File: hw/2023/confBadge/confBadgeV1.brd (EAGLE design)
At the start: 96.5 x 78.7 mm, 70 parts, among them J1 10118192-0002LF, Q1 8/16/20MHz, U1 ATMEGA328, U10 WS2812-2020, U11 WS2812-2020, U12 WS2812-2020, U13 WS2812-2020, U14 WS2812-2020, U15 WS2812-2020, U16 WS2812-2020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

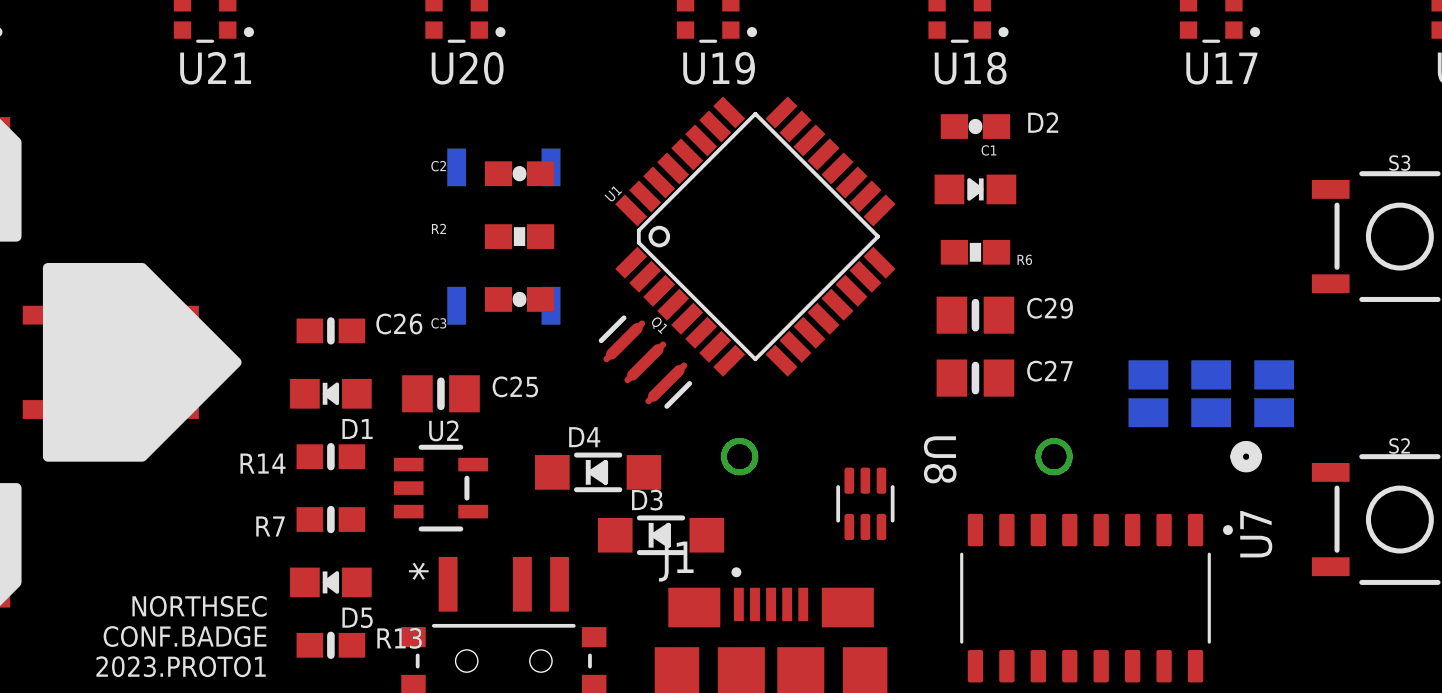
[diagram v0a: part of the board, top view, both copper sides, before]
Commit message: Tested monochrome bitmap
Added Rao to the back of the confBadge for testing
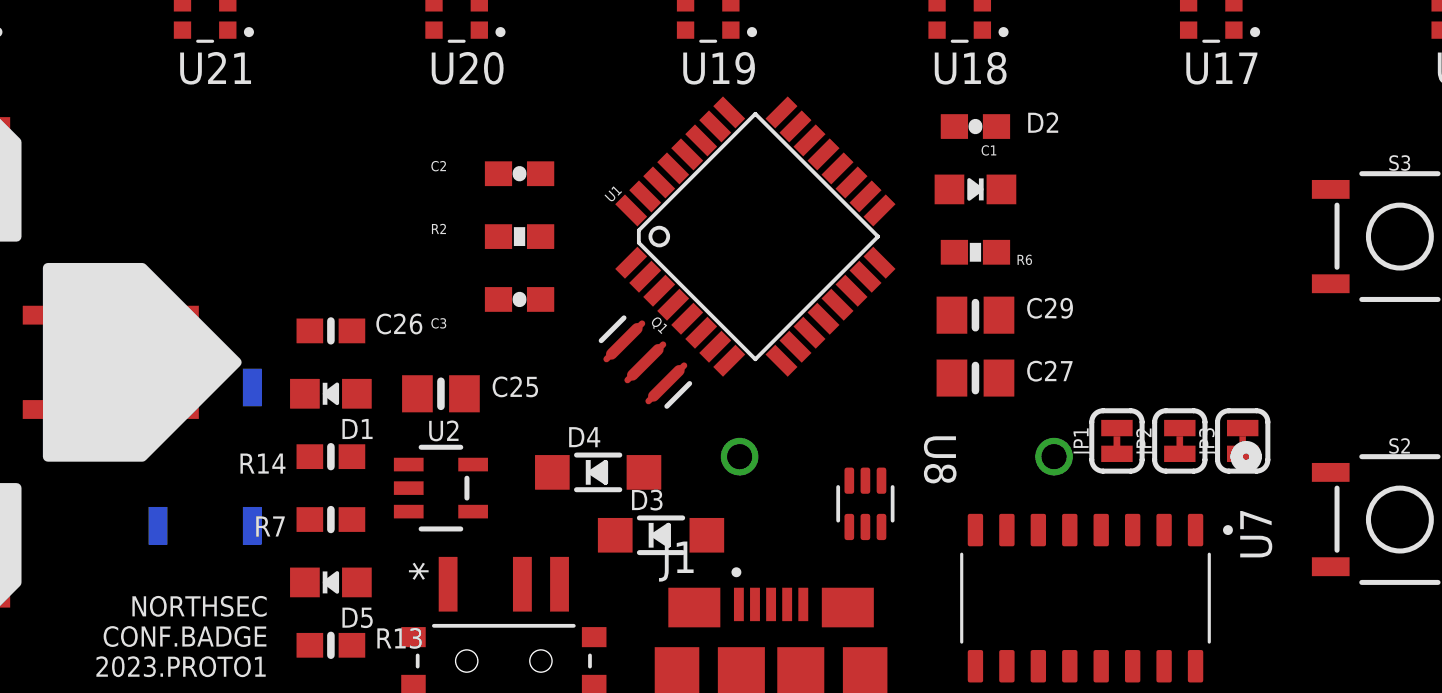
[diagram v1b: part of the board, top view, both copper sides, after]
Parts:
- removed SJ1, SJ2, SJ3: (no value), jumper:SJ
- added JP1, JP2, JP3: JUMPER-SMT_2_NC_TRACE_SILK, SparkFun-Jumpers:SMT-JUMPER_2_NC_TRACE_SILK
- moved S1 15.0 mm to (25.4, 10.2)
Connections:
- net CH340_DTR: now also JP1.2; no longer SJ1.2
- net CH340_RX: now also JP2.2; no longer SJ2.2
- net CH340_TX: now also JP3.2; no longer SJ3.2
- net DTR: now also JP1.1; no longer SJ1.1
- net RXI: now also JP3.1; no longer SJ3.1
- net TXO: now also JP2.1; no longer SJ2.1
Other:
- board text added: "Connect the badge with other participants to unlock more animations Go to the soldering village to add a screen to your badge"
- board text added: "QUESTS [1] [2]"
- board text removed: "C:/Users/lambert/Documents/GitHub/nsec-badge-dev/hw/2023/confBadge/reference/dear_leader-monotoneMed(100).bmp"

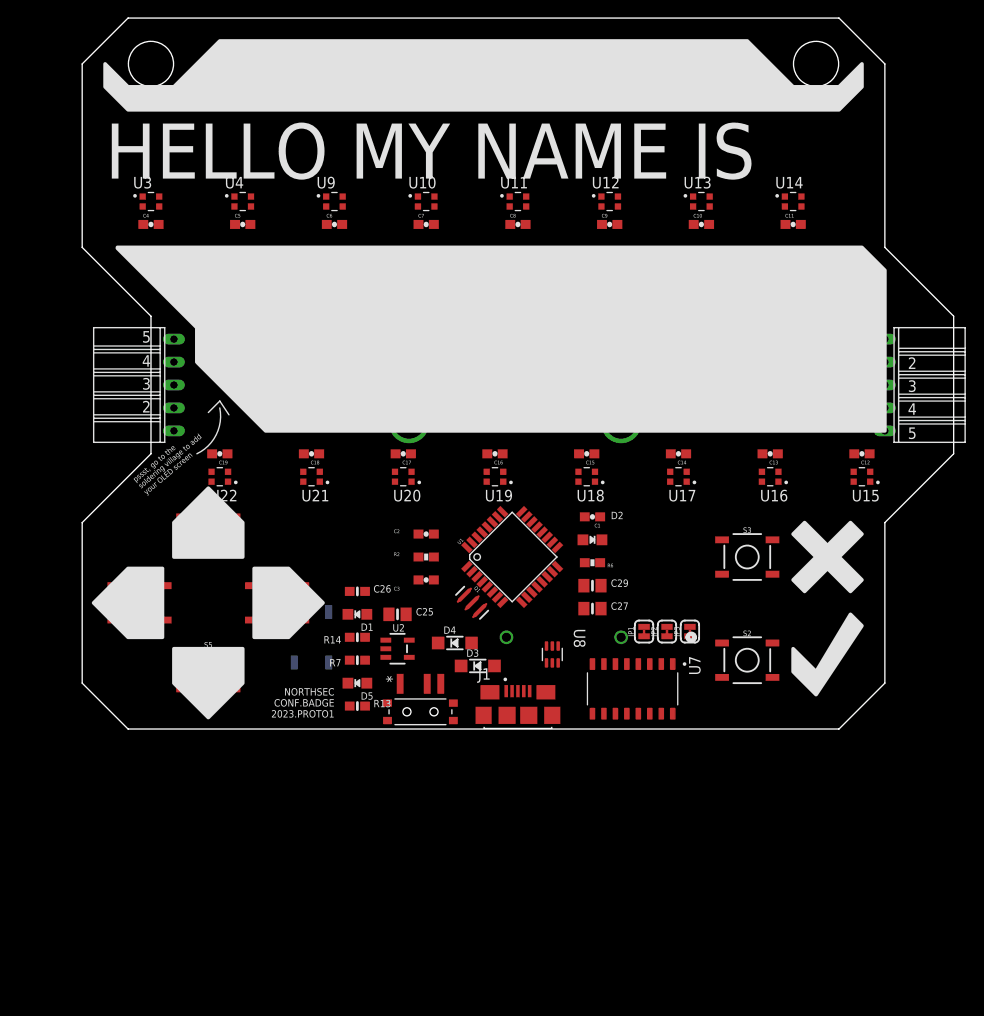
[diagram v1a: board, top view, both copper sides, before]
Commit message: finished routing layout
- added soldering village track
(1) through-hole + smd led at the top
(2) oled
(3) 2 button at the bottom right
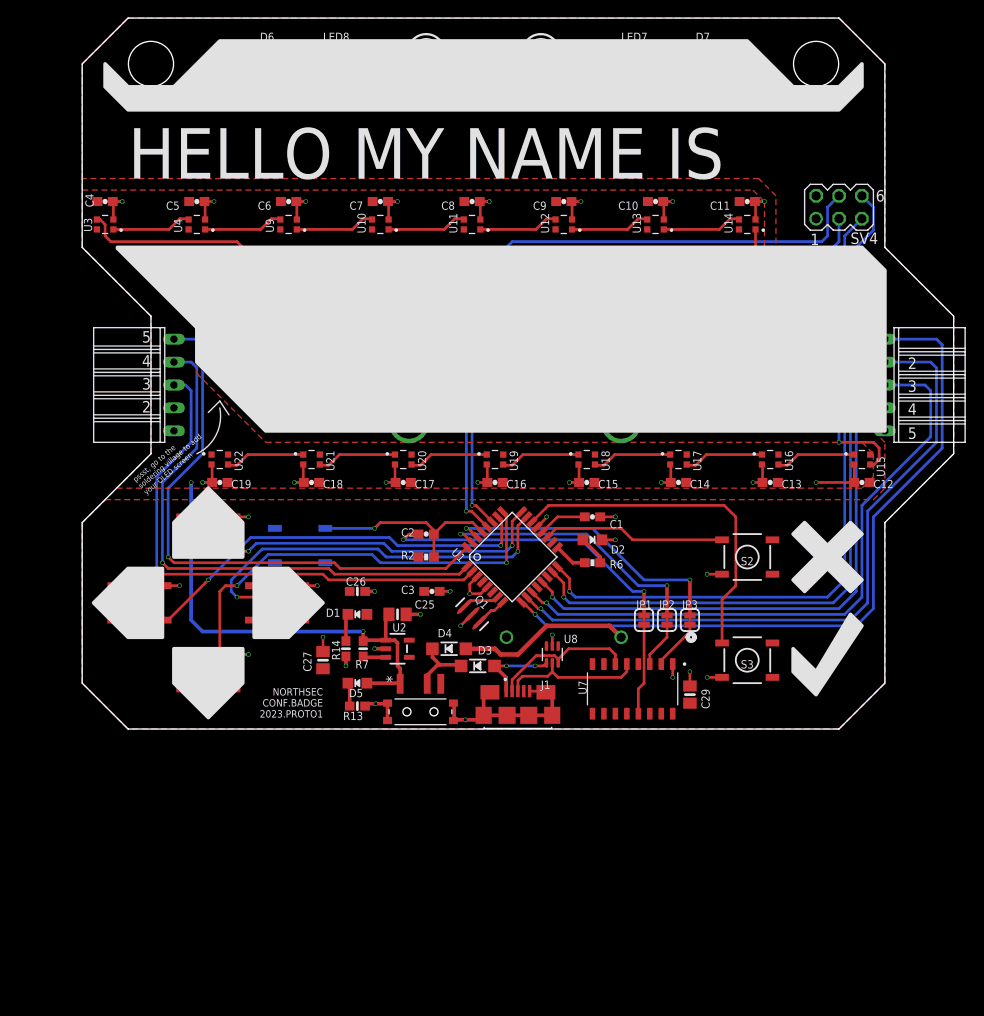
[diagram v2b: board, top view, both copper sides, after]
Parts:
- added D6, D7: NC, microbuilder:CHIPLED_0805_NOOUTLINE
- added LED2, LED3: NC, led:LED3MM
- added LED7, LED8: NC, led:CHIPLED_1206
- added R10, R11: NC, rcl:R1206W
- added R12, R15: NC, microbuilder:0603-NO
- added R3, R4: NC, rcl:0207/10
- added SV4: SAO, con-lstb:MA03-2
- S1: value (none) -> RST
- S2, S3: value (none) -> NC
- S4: value (none) -> U
- S5: value (none) -> D
- S6: value (none) -> L
- S7: value (none) -> R
- SV1: value (none) -> SYNCOUT
- SV2: value (none) -> SYNCIN
- SV3: value (none) -> OLED
- moved C27 30.4 mm to (26.7, 7.62), turned to 90 degrees
- moved C29 16.2 mm to (67.3, 3.81), turned to 90 degrees
- moved S2 11.4 mm to (73.7, 19.1), turned to 180 degrees
- moved S3 11.4 mm to (73.7, 7.62), turned to 180 degrees
- moved S1 10.2 mm to (24.1, 20.3), turned to 180 degrees
- moved C5 5.68 mm to (12.7, 58.4), turned to 180 degrees
- moved C6 5.68 mm to (22.9, 58.4), turned to 180 degrees
- moved U4 5.68 mm to (12.7, 55.9), turned to 180 degrees
- moved U9 5.68 mm to (22.9, 55.9), turned to 180 degrees
- moved C4 5.68 mm to (2.54, 58.4), turned to 180 degrees
- moved U3 5.68 mm to (2.54, 55.9), turned to 180 degrees
- moved C10 5.68 mm to (63.5, 58.4), turned to 180 degrees
- moved C11 5.68 mm to (73.7, 58.4), turned to 180 degrees
- moved C7 5.68 mm to (33.0, 58.4), turned to 180 degrees
- moved C8 5.68 mm to (43.2, 58.4), turned to 180 degrees
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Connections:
- removed net BTN4: U1.26
- removed net BTNB: U1.19
- removed net D7: SV1.3
- new net N$18: D6.A, R12.2
- new net N$19: LED2.A, R3.2
- new net N$21: LED3.A, R4.2
- new net N$22: D7.A, R15.2
- new net N$25: LED8.A, R10.1
- new net N$26: LED7.A, R11.1
- new net SAO_IO1: SV4.6, U1.15
- new net SAO_IO2: SV4.5, U1.16
- net 3.3V: now also R10.2, R11.2, R12.1, R15.1, R3.1, R4.1, SV4.2
- net BTN_B: now also U1.19
- net BTN_L: now also U1.26
- net GND: now also D6.C, D7.C, LED2.K, LED3.K, LED7.C, LED8.C, SV4.1
- net SCL: now also SV4.3
- net SDA: now also SV4.4
- net SIG_OUT3: now also SV1.3
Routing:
- net NEOPIX: track 0.00 -> 159.1 mm, vias 0 -> 2
- net GND: track 0.00 -> 116.2 mm, vias 0 -> 42
- net SDA: track 0.00 -> 102.6 mm, vias 0 -> 1
- net SCL: track 0.00 -> 102.3 mm, vias 0 -> 3
- net SAO_IO1: track 0.00 -> 80.9 mm, vias 0 -> 1
- net SIG_OUT1: track 0.00 -> 79.8 mm, vias 0 -> 1
- net SAO_IO2: track 0.00 -> 75.6 mm, vias 0 -> 1
- net SIG_OUT2: track 0.00 -> 74.8 mm, vias 0 -> 1
- net SIG_OUT3: track 0.00 -> 69.7 mm, vias 0 -> 1
- net SIG_IN1: track 0.00 -> 63.1 mm, vias 0 -> 1
- net SIG_IN2: track 0.00 -> 60.6 mm, vias 0 -> 1
- net SIG_IN3: track 0.00 -> 59.3 mm, vias 0 -> 1
- net BTN_D: track 0.00 -> 51.6 mm, vias 0 -> 2
- net VDD: track 0.00 -> 51.5 mm, vias 0 -> 2
- net BTN_R: track 0.00 -> 48.5 mm, vias 0 -> 2
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- added copper zone on layer 1, net 3.3V
- added copper zone on layer 16, net GND
- added copper zone on layer 1, net VDD

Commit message: Added ISP header
ISP header added for programming bootloader
and adjusted top silkscreen to show footprint for soldering village activity
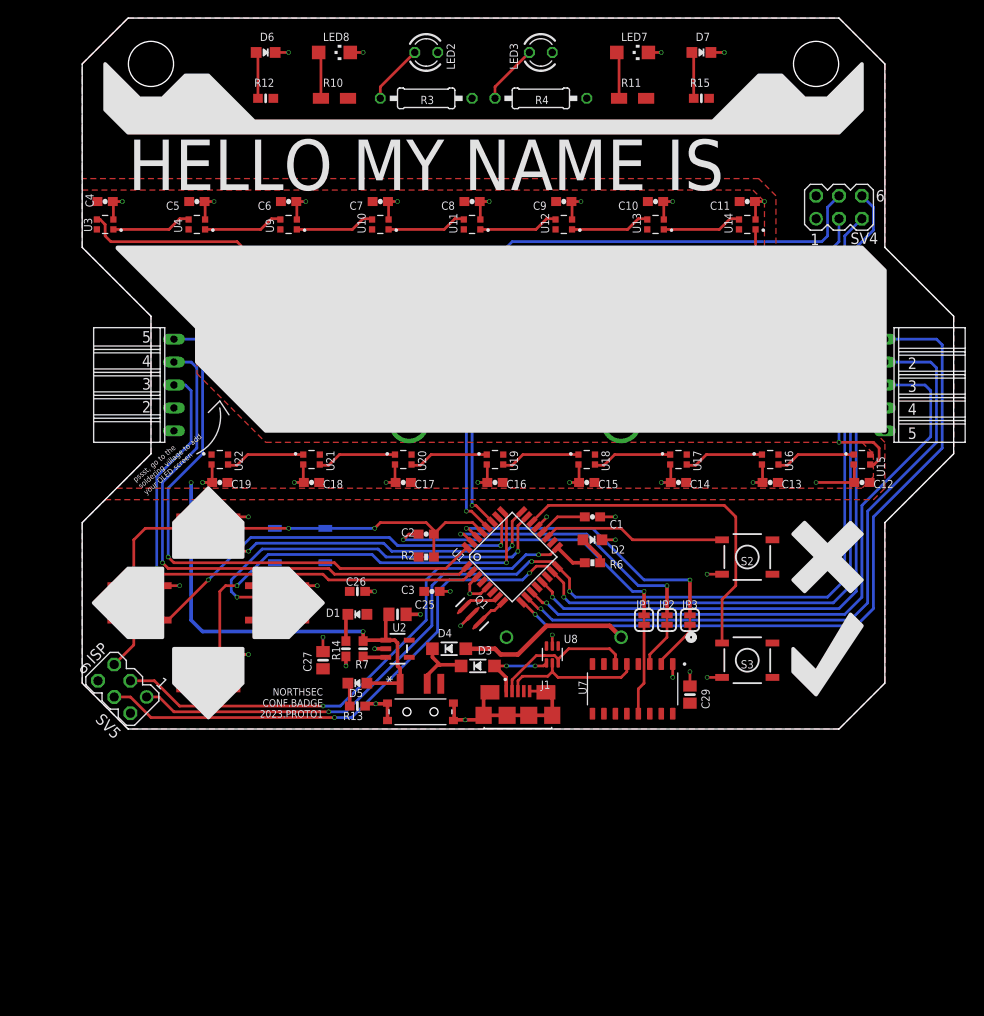
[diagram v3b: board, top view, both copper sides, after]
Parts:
- added SV5: ICSP, con-lstb:MA03-2
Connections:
- net 3.3V: now also SV5.2
- net DBG_LED: now also SV5.3
- net GND: now also SV5.6
- net RESET: now also SV5.5
- net SAO_IO1: now also SV5.4
- net SAO_IO2: now also SV5.1
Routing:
- net SAO_IO1: track 80.9 -> 140.2 mm, vias 1 -> 3
- net DBG_LED: track 3.72 -> 62.1 mm, vias 0 -> 2
- net SAO_IO2: track 75.6 -> 131.5 mm, vias 1 -> 3
- net RESET: track 21.9 -> 58.4 mm, vias 1 -> 2
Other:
- board text added: "ISP"
